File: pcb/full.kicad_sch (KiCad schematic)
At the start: 116 parts, among them SW1 SW_PUSH, SW10 SW_PUSH, SW11 SW_PUSH, SW12 SW_PUSH, SW13 SW_PUSH, SW14 SW_PUSH, SW15 SW_PUSH, SW16 SW_PUSH, SW17 SW_PUSH, SW18 SW_PUSH, SW19 SW_PUSH, SW2 SW_PUSH, SW20 SW_PUSH, SW21 SW_PUSH, SW22 SW_PUSH, SW23 SW_PUSH, SW24 SW_PUSH, SW25 SW_PUSH, SW26 SW_PUSH, SW27 SW_PUSH, SW28 SW_PUSH, SW29 SW_PUSH, SW3 SW_PUSH, SW30 SW_PUSH, SW31 SW_PUSH, SW32 SW_PUSH, SW33 SW_PUSH, SW34 SW_PUSH, SW35 SW_PUSH, SW36 SW_PUSH, SW37 SW_PUSH, SW38 SW_PUSH, SW39 SW_PUSH, SW4 SW_PUSH, SW40 SW_PUSH, SW5 SW_PUSH, SW6 SW_PUSH, SW7 SW_PUSH, SW8 SW_PUSH, SW9 SW_PUSH, U1 xiao-ble, U2 xiao-ble

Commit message: v2
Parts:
- removed BR5, BR6, BR7, BR8: Breakaway, kbd:Breakaway_Tabs, symbol Mechanical:MountingHole
- added BATTCONN3, BATTCONN4: Conn_01x02_Female, pica:JST_PH_S2B-PH-K_1x02_P2.00mm, symbol Connector:Conn_01x02_Female
- added RE3, RE4: RotaryEncoder_Switch, pica:RotaryEncoder_EC11, symbol Device:RotaryEncoder_Switch
- BATTCONN1, BATTCONN2: footprint pica:JST_PH_S2B-PH-K_1x02_P2.00mm_Horizontal -> pica:JST_PH_S2B-PH-K_1x02_P2.00mm
- H1, H10, H11, H12, H2, H3, H4, H5, H8, H9: footprint kbd:M2_HOLE_v2 -> pica:spacer_m2_3.4
- H13, H14, H6, H7: footprint kbd:M2_Hole_TH -> kbd:thread_m2
- SW1, SW10, SW11, SW12, SW13, SW14, SW15, SW16, SW17, SW18, SW19, SW2, SW21, SW22, SW23, SW24, SW25, SW26, SW27, SW28, SW29, SW3, SW30, SW31, SW32, SW33, SW34, SW35, SW36, SW37, SW38, SW39, SW4, SW5, SW6, SW7, SW8, SW9: footprint pica:CherryMX_Hotswap -> pica:CherryMX_Hotswap_ChocV2
- SW20, SW40: footprint pica:CherryMX_Hotswap_1.5 -> pica:CherryMX_Hotswap_ChocV2_1.5
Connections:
- net BATT: now also BATTCONN3.1 (Pin_1)
- net BATT_r: now also BATTCONN4.1 (Pin_1)
- net ENCA: now also RE3.A
- net ENCA_r: now also RE4.A
- net ENCB: now also RE3.B
- net ENCB_r: now also RE4.B
- net GND: now also BATTCONN3.2 (Pin_2), RE3.C; no longer BATTCONN2.2 (Pin_2), RE2.C, U2.13 (GND), U2.18 (GND), U2.20 (GND), USB2.1 (GND), USB2.12 (GND)
- new net GNDA: BATTCONN2.2 (Pin_2), BATTCONN4.2 (Pin_2), RE2.C, RE4.C, U2.13 (GND), U2.18 (GND), U2.20 (GND), USB2.1 (GND), USB2.12 (GND)
- no-connect marks 28 -> 32
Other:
- moved on the sheet: BATTCONN1, BATTCONN2, BATTSW1, BATTSW2

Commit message: remove second encoder
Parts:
- removed RE3, RE4: RotaryEncoder_Switch, pica:RotaryEncoder_EC11, symbol Device:RotaryEncoder_Switch
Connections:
- no-connect marks 32 -> 28
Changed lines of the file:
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@@
   (no_connect (at 142.24 55.88))
   (no_connect (at 347.98 33.02))
-  (no_connect (at 69.85 251.46))
   (no_connect (at 68.58 22.86))
-  (no_connect (at 69.85 246.38))
   (no_connect (at 297.18 33.02))
   (no_connect (at 274.32 57.15))
@@
   (no_connect (at 265.43 184.15))
   (no_connect (at 142.24 48.26))
-  (no_connect (at 275.59 255.27))
   (no_connect (at 275.59 231.14))
-  (no_connect (at 275.59 250.19))
   (no_connect (at 69.85 233.68))
   (no_connect (at 66.04 22.86))
@@
     (stroke (width 0) (type default) (color 0 0 0 0))
   )
-  (wire (pts (xy 260.35 252.73) (xy 248.92 252.73))
-    (stroke (width 0) (type default) (color 0 0 0 0))
-  )
   (wire (pts (xy 260.35 120.65) (xy 260.35 123.19))
     (stroke (width 0) (type default) (color 0 0 0 0))
@@
     (stroke (width 0) (type default) (color 0 0 0 0))
   )
-  (wire (pts (xy 54.61 248.92) (xy 43.18 248.92))
-    (stroke (width 0) (type default) (color 0 0 0 0))
-  )
   (wire (pts (xy 135.89 152.4) (xy 135.89 153.67))
     (stroke (width 0) (type default) (color 0 0 0 0))
@@
     )
   )
-  (global_label "ENCB_r" (shape input) (at 260.35 255.27 180) (fields_autoplaced)
-    (effects (font (size 1.27 1.27)) (justify right))
-    (property "Intersheet References" "${INTERSHEET_REFS}" (id 0) (at 251.1636 255.1906 0)
-      (effects (font (size 1.27 1.27)) (justify right) hide)
-    )
-  )
   (global_label "col0_r" (shape input) (at 254 33.02 180) (fields_autoplaced)
     (effects (font (size 1.27 1.27)) (justify right))
@@
     )
   )
-  (global_label "ENCA" (shape input) (at 54.61 246.38 180) (fields_autoplaced)
-    (effects (font (size 1.27 1.27)) (justify right))
-    (property "Intersheet References" "${INTERSHEET_REFS}" (id 0) (at 47.3588 246.3006 0)
-      (effects (font (size 1.27 1.27)) (justify right) hide)
-    )
-  )
   (global_label "row0_r" (shape input) (at 297.18 40.64 0) (fields_autoplaced)
     (effects (font (size 1.27 1.27)) (justify left))
@@
     )
   )
-  (global_label "ENCA_r" (shape input) (at 260.35 250.19 180) (fields_autoplaced)
-    (effects (font (size 1.27 1.27)) (justify right))
-    (property "Intersheet References" "${INTERSHEET_REFS}" (id 0) (at 251.345 250.1106 0)
-      (effects (font (size 1.27 1.27)) (justify right) hide)
-    )
-  )
   (global_label "col4" (shape input) (at 48.26 40.64 180) (fields_autoplaced)
     (effects (font (size 1.27 1.27)) (justify right))
@@
     )
   )
-  (global_label "ENCB" (shape input) (at 54.61 251.46 180) (fields_autoplaced)
-    (effects (font (size 1.27 1.27)) (justify right))
-    (property "Intersheet References" "${INTERSHEET_REFS}" (id 0) (at 47.1774 251.3806 0)
-      (effects (font (size 1.27 1.27)) (justify right) hide)
-    )
-  )
   (global_label "col1" (shape input) (at 90.17 78.74 90) (fields_autoplaced)
     (effects (font (size 1.27 1.27)) (justify left))
@@
     (pin "2")
   )
-  (symbol (lib_id "Device:RotaryEncoder_Switch") (at 62.23 248.92 0) (unit 1)
-    (in_bom yes) (on_board yes) (fields_autoplaced)
-    (property "Reference" "RE3" (id 0) (at 62.23 238.76 0))
-    (property "Value" "RotaryEncoder_Switch" (id 1) (at 62.23 241.3 0))
-    (property "Footprint" "pica:RotaryEncoder_EC11" (id 2) (at 58.42 244.856 0)
-      (effects (font (size 1.27 1.27)) hide)
-    )
-    (property "Datasheet" "~" (id 3) (at 62.23 242.316 0)
-      (effects (font (size 1.27 1.27)) hide)
-    )
-    (pin "A")
-    (pin "B")
-    (pin "C")
-    (pin "S1")
-    (pin "S2")
-  )
   (symbol (lib_id "Switch:SW_SPDT") (at 260.35 181.61 0) (unit 1)
     (in_bom yes) (on_board yes) (fields_autoplaced)
@@
     (pin "2")
   )
-  (symbol (lib_id "Device:RotaryEncoder_Switch") (at 267.97 252.73 0) (unit 1)
-    (in_bom yes) (on_board yes) (fields_autoplaced)
-    (property "Reference" "RE4" (id 0) (at 267.97 242.57 0))
-    (property "Value" "RotaryEncoder_Switch" (id 1) (at 267.97 245.11 0))
-    (property "Footprint" "pica:RotaryEncoder_EC11" (id 2) (at 264.16 248.666 0)
-      (effects (font (size 1.27 1.27)) hide)
-    )
-    (property "Datasheet" "~" (id 3) (at 267.97 246.126 0)
-      (effects (font (size 1.27 1.27)) hide)
-    )
-    (pin "A")
-    (pin "B")
-    (pin "C")
-    (pin "S1")
-    (pin "S2")
-  )
   (symbol (lib_id "kbd:SW_PUSH") (at 328.93 93.98 0) (unit 1)
     (in_bom yes) (on_board yes) (fields_autoplaced)
@@
     (pin "2")
   )
-  (symbol (lib_id "power:GNDA") (at 248.92 252.73 0) (unit 1)
-    (in_bom yes) (on_board yes)
-    (property "Reference" "#PWR0109" (id 0) (at 248.92 259.08 0)
-      (effects (font (size 1.27 1.27)) hide)
-    )
-    (property "Value" "GNDA" (id 1) (at 245.11 254 0))
-    (property "Footprint" "" (id 2) (at 248.92 252.73 0)
-      (effects (font (size 1.27 1.27)) hide)
-    )
-    (property "Datasheet" "" (id 3) (at 248.92 252.73 0)
-      (effects (font (size 1.27 1.27)) hide)
-    )
-    (pin "1")
-  )
   (symbol (lib_id "power:GND") (at 66.04 60.96 0) (mirror y) (unit 1)
     (in_bom yes) (on_board yes)
@@
     (pin "2")
   )
-  (symbol (lib_id "power:GND") (at 43.18 248.92 0) (unit 1)
-    (in_bom yes) (on_board yes)
-    (property "Reference" "#PWR025" (id 0) (at 43.18 255.27 0)
-      (effects (font (size 1.27 1.27)) hide)
-    )
-    (property "Value" "GND" (id 1) (at 39.37 250.19 0))
-    (property "Footprint" "" (id 2) (at 43.18 248.92 0)
-      (effects (font (size 1.27 1.27)) hide)
-    )
-    (property "Datasheet" "" (id 3) (at 43.18 248.92 0)
-      (effects (font (size 1.27 1.27)) hide)
-    )
-    (pin "1")
-  )
   (symbol (lib_id "Device:D_Small") (at 260.35 138.43 90) (unit 1)
     (in_bom yes) (on_board yes) (fields_autoplaced)
@@
       (reference "#PWR022") (unit 1) (value "VDD") (footprint "")
     )
-    (path "/f88f48cb-e07c-4650-bfa1-bf599fed2bc6"
-      (reference "#PWR025") (unit 1) (value "GND") (footprint "")
-    )
     (path "/f4975bd7-6b39-42eb-ae54-dc0565bc4f70"
       (reference "#PWR0101") (unit 1) (value "GNDA") (footprint "")
@@
       (reference "#PWR0108") (unit 1) (value "GNDA") (footprint "")
     )
-    (path "/e1bea627-a663-4344-b15f-6fada62d419e"
-      (reference "#PWR0109") (unit 1) (value "GNDA") (footprint "")
-    )
     (path "/15d4c5c2-186a-41ec-9167-604695d5a8ac"
       (reference "#PWR0110") (unit 1) (value "GNDA") (footprint "")
@@
       (reference "RE2") (unit 1) (value "RotaryEncoder_Switch") (footprint "pica:RotaryEncoder_EC11")
     )
-    (path "/4da36a14-1f04-4190-adee-471beedc6349"
-      (reference "RE3") (unit 1) (value "RotaryEncoder_Switch") (footprint "pica:RotaryEncoder_EC11")
-    )
-    (path "/7105cc4b-4f80-40a4-b299-ec6e69897a28"
-      (reference "RE4") (unit 1) (value "RotaryEncoder_Switch") (footprint "pica:RotaryEncoder_EC11")
-    )
     (path "/dfe7bca9-eacf-484d-9fb9-819b1262f86e"

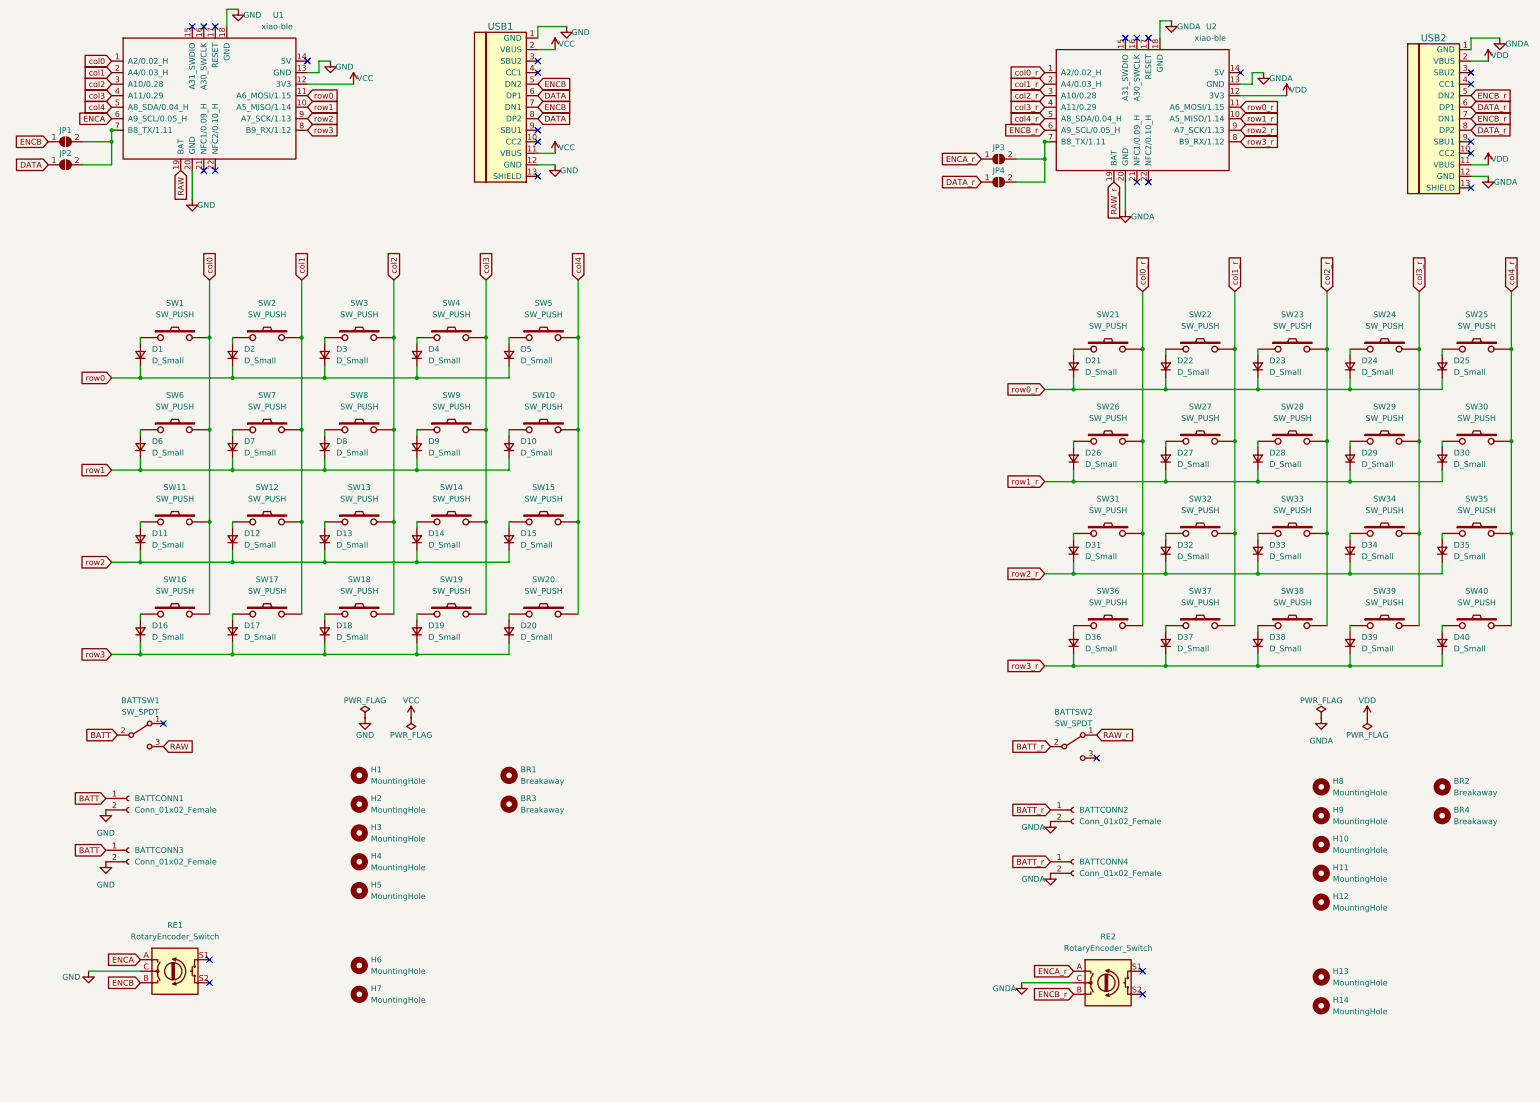
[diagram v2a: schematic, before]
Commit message: migrate to my component library
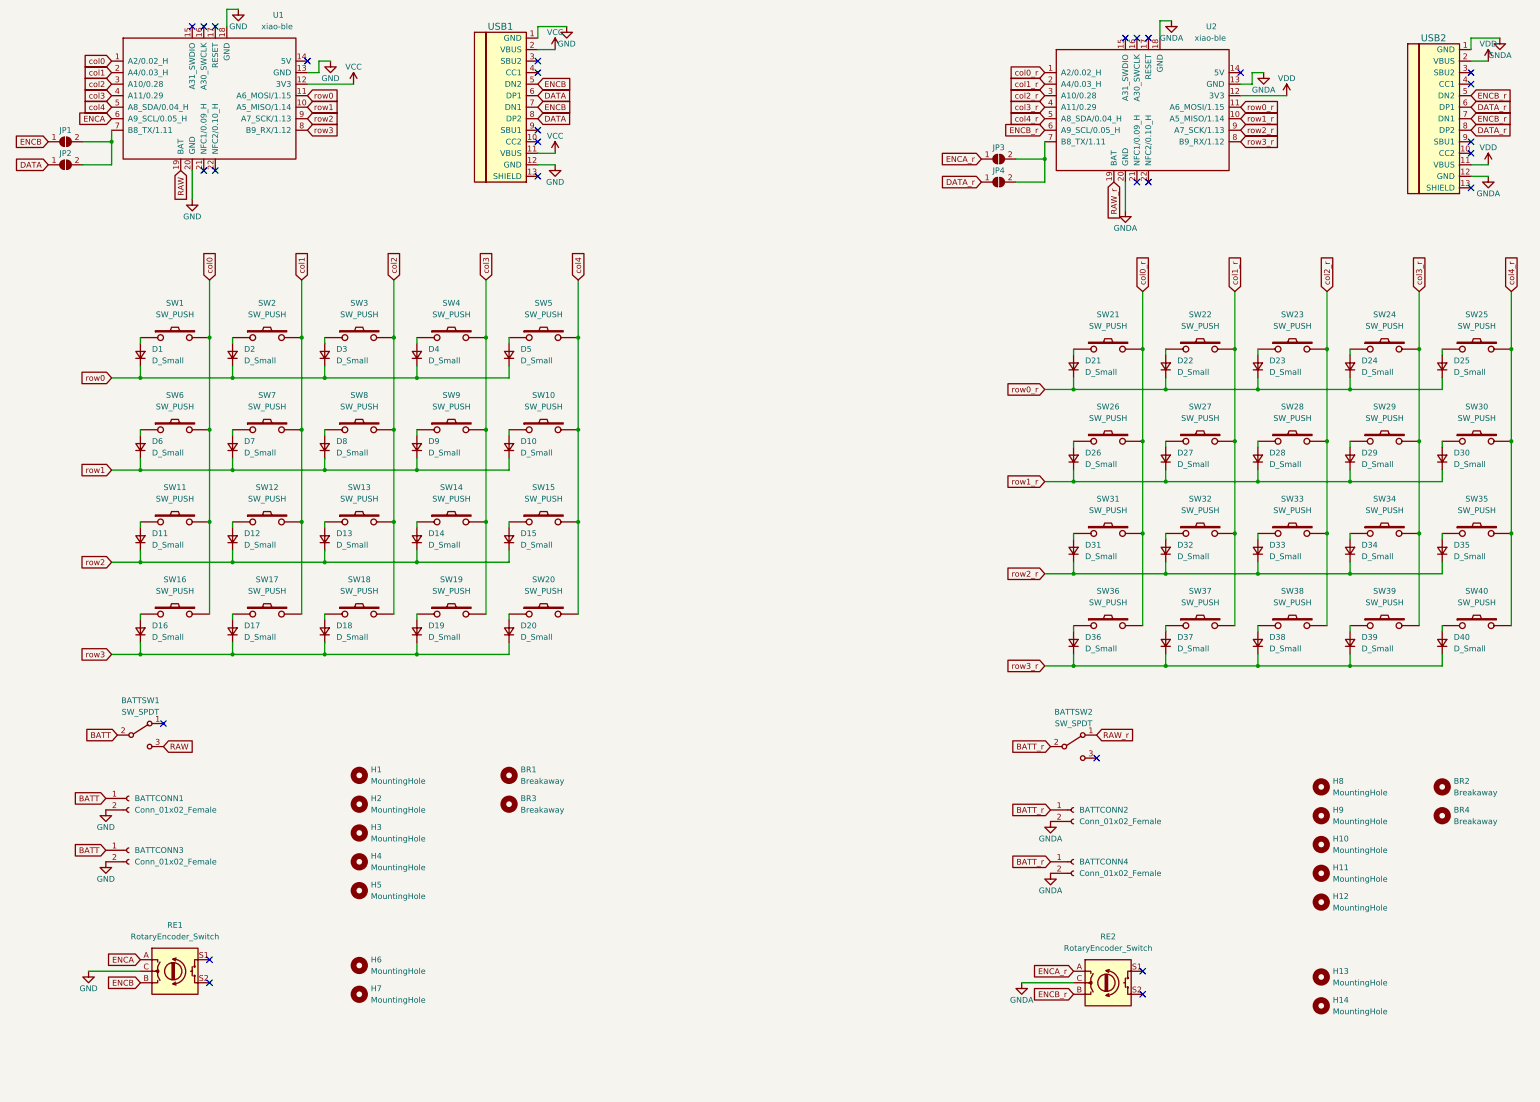
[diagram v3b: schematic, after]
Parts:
- BATTCONN1, BATTCONN2, BATTCONN3, BATTCONN4: footprint pica:JST_PH_S2B-PH-K_1x02_P2.00mm -> zzkeeb:Connector_JST-1x02-2.00mm
- BATTSW1, BATTSW2: footprint Button_Switch_SMD:SW_SPDT_PCM12 -> zzkeeb:Switch_SPDT-PCM12
- BR1, BR2, BR3, BR4: footprint kbd:Breakaway_Tabs -> zzkeeb:Hole_Breakaway-Tabs
- D1, D10, D11, D12, D13, D14, D15, D16, D17, D18, D19, D2, D20, D21, D22, D23, D24, D25, D26, D27, D28, D29, D3, D30, D31, D32, D33, D34, D35, D36, D37, D38, D39, D4, D40, D5, D6, D7, D8, D9: footprint pica:D3_SMD -> zzkeeb:Diode_1N4148-SOD123
- H1, H10, H11, H12, H2, H3, H4, H5, H8, H9: footprint pica:spacer_m2_3.4 -> zzkeeb:Hole_M2-spacer
- H13, H14, H6, H7: footprint kbd:thread_m2 -> zzkeeb:Hole_M2
- RE1, RE2: footprint pica:RotaryEncoder_EC11 -> zzkeeb:RotaryEncoder_EC11
- SW1, SW10, SW11, SW12, SW13, SW14, SW15, SW16, SW17, SW18, SW19, SW2, SW21, SW22, SW23, SW24, SW25, SW26, SW27, SW28, SW29, SW3, SW30, SW31, SW32, SW33, SW34, SW35, SW36, SW37, SW38, SW39, SW4, SW5, SW6, SW7, SW8, SW9: footprint pica:CherryMX_Hotswap_ChocV2 -> zzkeeb:Switch_MXChocV2-hotswap; symbol kbd:SW_PUSH -> zzkeeb:Switch
- SW20, SW40: footprint pica:CherryMX_Hotswap_ChocV2_1.5 -> zzkeeb:Switch_MXChocV2-hotswap-1.5; symbol kbd:SW_PUSH -> zzkeeb:Switch
- U1, U2: footprint pica:xiao-ble-tht -> zzkeeb:MCU_xiao-ble-tht; symbol kleeb-mcu:xiao-ble -> zzkeeb:MCU_xiao-ble
- USB1, USB2: footprint pica:HRO-TYPE-C-31-M-12-data -> zzkeeb:Connector_HRO-TYPE-C-31-M-12-data; symbol typec:HRO-TYPE-C-31-M-12 -> zzkeeb:Connector_HRO-TYPE-C-31-M-12
